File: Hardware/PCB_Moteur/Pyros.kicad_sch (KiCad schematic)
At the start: 33 parts, among them J8 Screw_Terminal_01x04, Q1 MMBT3904, Q2 SI7617DN-T1-GE3, Q3 SI5442DU-T1-GE3, Q4 SI5442DU-T1-GE3, U3 LM393

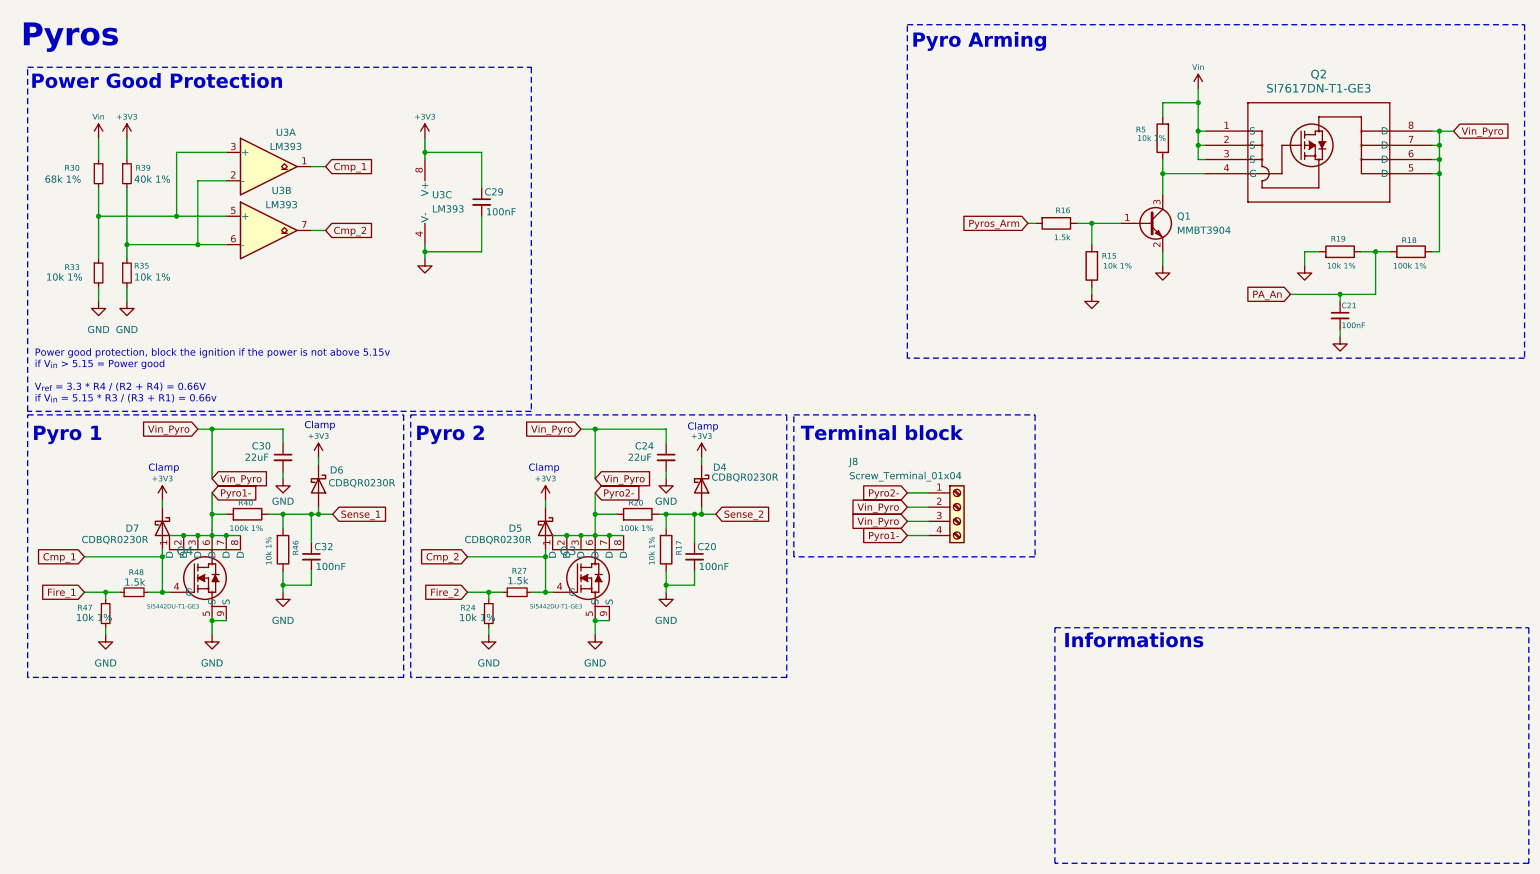
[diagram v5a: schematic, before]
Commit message: wip(moteur): reimport SI7617DN-T1-GE3 footprint + fix pads
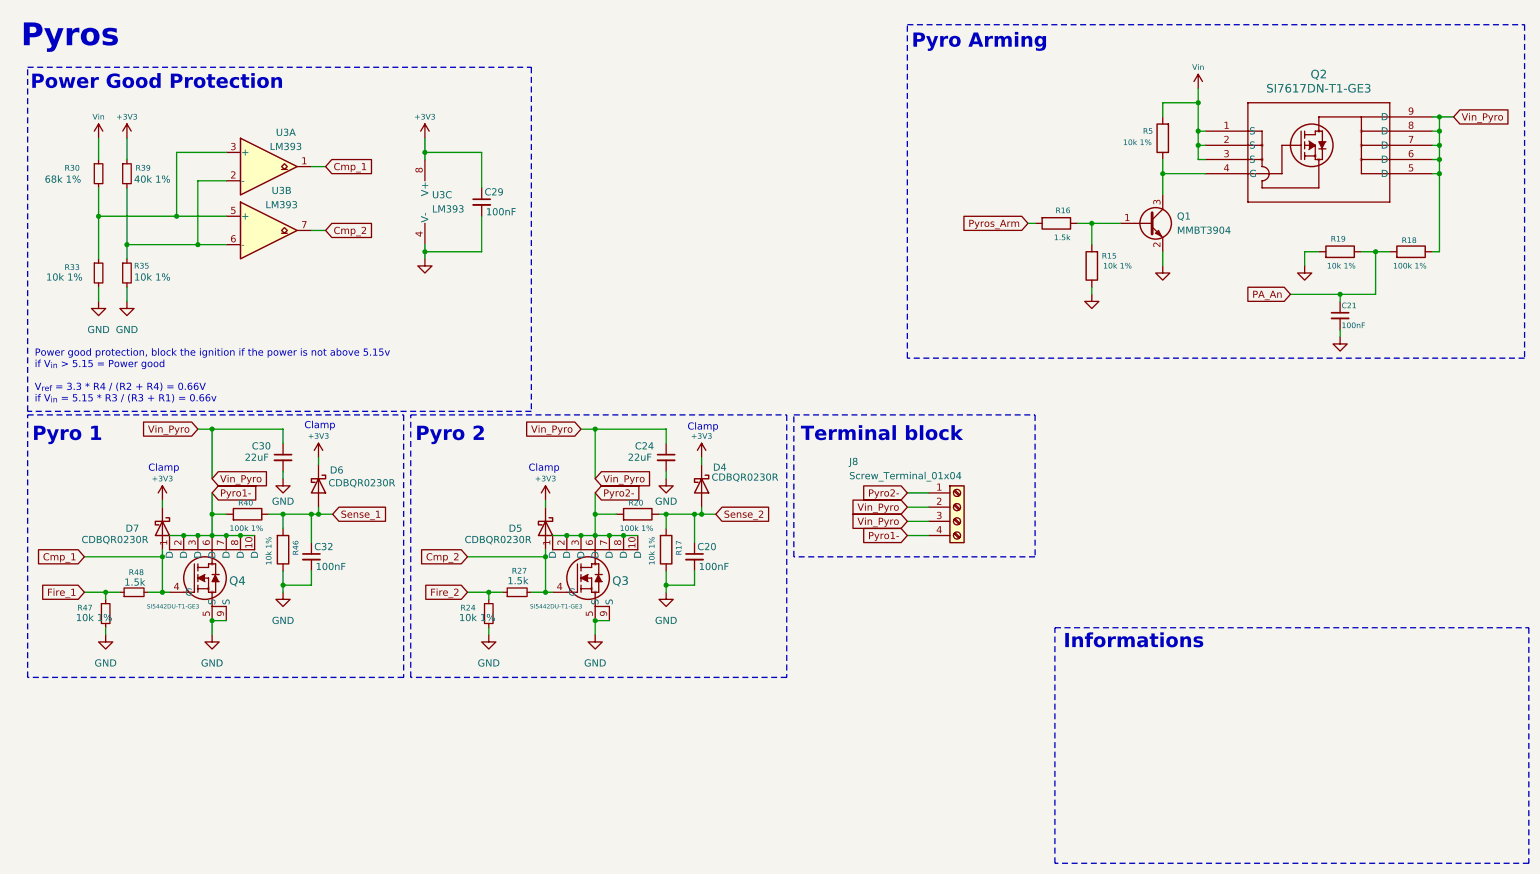
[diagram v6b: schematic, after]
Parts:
- Q2: footprint pcb_moteur:SI7617DN-T1-GE3 -> pcb_moteur:POWERPAK_1212-8_VIS
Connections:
- net Pyro1-: now also Q4.10 (D)
- net Pyro2-: now also Q3.10 (D)
- net Vin_Pyro: now also Q2.9 (D)
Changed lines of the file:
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@@
 	)
 	(junction
+		(at 266.7 30.48)
+		(diameter 0)
+		(color 0 0 0 0)
+	)
+	(junction
 		(at 113.03 105.41)
 		(diameter 0)
@@
 	)
 	(junction
+		(at 120.65 105.41)
+		(diameter 0)
+		(color 0 0 0 0)
+	)
+	(junction
 		(at 266.7 38.1)
 		(diameter 0)
@@
 	)
 	(junction
+		(at 52.07 105.41)
+		(diameter 0)
+		(color 0 0 0 0)
+	)
+	(junction
 		(at 128.27 114.3)
 		(diameter 0)
@@
 	(wire
 		(pts
+			(xy 120.65 105.41) (xy 123.19 105.41)
+		)
+		(stroke
+			(width 0)
+			(type default)
+		)
+	)
+	(wire
+		(pts
 			(xy 38.1 109.22) (xy 38.1 115.57)
 		)
@@
 	(wire
 		(pts
+			(xy 266.7 30.48) (xy 266.7 33.02)
+		)
+		(stroke
+			(width 0)
+			(type default)
+		)
+	)
+	(wire
+		(pts
 			(xy 95.25 36.83) (xy 85.09 36.83)
 		)
@@
 	(wire
 		(pts
-			(xy 266.7 33.02) (xy 269.24 33.02)
+			(xy 266.7 30.48) (xy 269.24 30.48)
 		)
 		(stroke
@@
 	(wire
 		(pts
+			(xy 52.07 105.41) (xy 54.61 105.41)
+		)
+		(stroke
+			(width 0)
+			(type default)
+		)
+	)
+	(wire
+		(pts
 			(xy 171.45 102.87) (xy 175.26 102.87)
 		)
@@
 	(wire
 		(pts
+			(xy 265.43 30.48) (xy 266.7 30.48)
+		)
+		(stroke
+			(width 0)
+			(type default)
+		)
+	)
+	(wire
+		(pts
 			(xy 115.57 97.79) (xy 115.57 101.6)
 		)
@@
 	(global_label "Vin_Pyro"
 		(shape input)
-		(at 269.24 33.02 0)
+		(at 269.24 30.48 0)
 		(fields_autoplaced yes)
 		(effects
@@
 		)
 		(property "Intersheetrefs" "${INTERSHEET_REFS}"
-			(at 280.208 33.02 0)
+			(at 280.208 30.48 0)
 			(effects
 				(font
@@
 		(dnp no)
 		(property "Reference" "R5"
-			(at 212.344 32.766 0)
+			(at 213.614 33.02 0)
 			(effects
 				(font
@@
 		)
 		(property "Value" "10k 1%"
-			(at 212.598 34.29 0)
+			(at 210.058 35.052 0)
 			(effects
 				(font
@@
 	)
 	(symbol
+		(lib_name "SI5442DU-T1-GE3_1")
 		(lib_id "pcb_moteur:SI5442DU-T1-GE3")
 		(at 107.95 115.57 0)
@@
 		(dnp no)
 		(property "Reference" "Q3"
-			(at 109.22 108.204 0)
+			(at 118.618 113.538 0)
 			(effects
 				(font
@@
 		(pin "2"
 		)
+		(pin "10"
+		)
 		(instances
 			(project "PCB_moteur"
@@
 			)
 		)
-		(property "Footprint" "pcb_moteur:SI7617DN-T1-GE3"
+		(property "Footprint" "pcb_moteur:POWERPAK_1212-8_VIS"
 			(at 224.79 33.02 0)
 			(effects
@@
 			)
 		)
-		(property "Datasheet" "https://www.digikey.ca/en/products/detail/vishay-siliconix/SI7617DN-T1-GE3/2441735"
+		(property "Datasheet" "https://www.vishay.com/doc?65164"
 			(at 224.79 33.02 0)
 			(effects
@@
 		(pin "6"
 		)
+		(pin "9"
+		)
 		(instances
 			(project ""
@@
 		(dnp no)
 		(property "Reference" "Q4"
-			(at 40.64 108.204 0)
+			(at 50.038 113.538 0)
 			(effects
 				(font
@@
 		(pin "6"
 		)
+		(pin "10"
+		)
 		(instances

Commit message: fix : BOM errors, change cutoff freq for moteur, minor fixes for GSE
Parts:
- R16, R27, R48: DigiKey_Part_Number P1.5KDBCT-ND -> 311-1.50KCRCT-ND; Manufacturer_Part_Number ERA-3AEB152V -> RC0805FR-071K5L
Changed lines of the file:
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@@
 			)
 		)
-		(property "Datasheet" "https://www.vishay.com/doc?65164"
+		(property "Datasheet" "https://www.digikey.com/en/products/detail/vishay-siliconix/SI7617DN-T1-GE3/2441735?s=N4IgTCBcDaIMoEkDsA2AjEgIgOQLQBU1cBxAUQGYBhfXbTEAXQF8g"
 			(at 224.79 33.02 0)
 			(effects
@@
 			)
 		)
-		(property "Datasheet" "https://www.digikey.ca/en/products/detail/panasonic-electronic-components/ERA-3AEB152V/1465858"
+		(property "Datasheet" "https://www.digikey.ca/en/products/detail/yageo/RC0805FR-071K5L/727496"
 			(at 101.6 115.57 0)
 			(effects
@@
 			)
 		)
-		(property "DigiKey_Part_Number" "P1.5KDBCT-ND"
+		(property "DigiKey_Part_Number" "311-1.50KCRCT-ND"
 			(at 101.6 115.57 90)
 			(effects
@@
 			)
 		)
-		(property "Manufacturer_Part_Number" "ERA-3AEB152V"
+		(property "Manufacturer_Part_Number" "RC0805FR-071K5L"
 			(at 101.6 115.57 90)
 			(effects
@@
 			)
 		)
-		(property "Datasheet" "https://www.digikey.ca/en/products/detail/panasonic-electronic-components/ERA-3AEB152V/1465858"
+		(property "Datasheet" "https://www.digikey.ca/en/products/detail/yageo/RC0805FR-071K5L/727496"
 			(at 198.12 49.53 0)
 			(effects
@@
 			)
 		)
-		(property "DigiKey_Part_Number" "P1.5KDBCT-ND"
+		(property "DigiKey_Part_Number" "311-1.50KCRCT-ND"
 			(at 198.12 49.53 90)
 			(effects
@@
 			)
 		)
-		(property "Manufacturer_Part_Number" "ERA-3AEB152V"
+		(property "Manufacturer_Part_Number" "RC0805FR-071K5L"
 			(at 198.12 49.53 90)
 			(effects
@@
 			)
 		)
-		(property "Datasheet" "https://www.digikey.ca/en/products/detail/panasonic-electronic-components/ERA-3AEB152V/1465858"
+		(property "Datasheet" "https://www.digikey.ca/en/products/detail/yageo/RC0805FR-071K5L/727496"
 			(at 33.02 115.57 0)
 			(effects
@@
 			)
 		)
-		(property "DigiKey_Part_Number" "P1.5KDBCT-ND"
+		(property "DigiKey_Part_Number" "311-1.50KCRCT-ND"
 			(at 33.02 115.57 90)
 			(effects
@@
 			)
 		)
-		(property "Manufacturer_Part_Number" "ERA-3AEB152V"
+		(property "Manufacturer_Part_Number" "RC0805FR-071K5L"
 			(at 33.02 115.57 90)
 			(effects

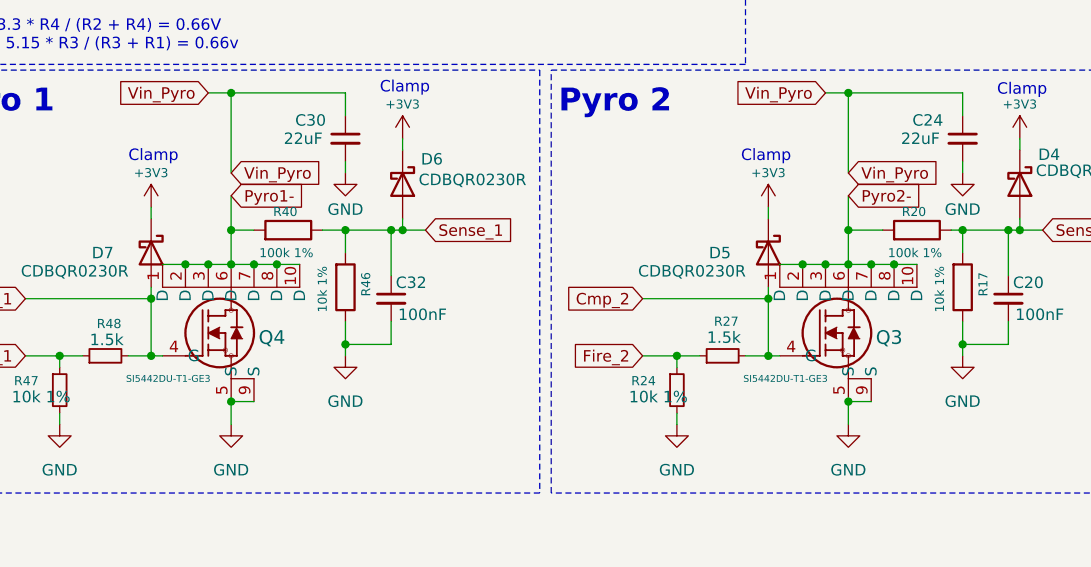
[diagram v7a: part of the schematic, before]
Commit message: fix(moteur): mosfet pyros pads
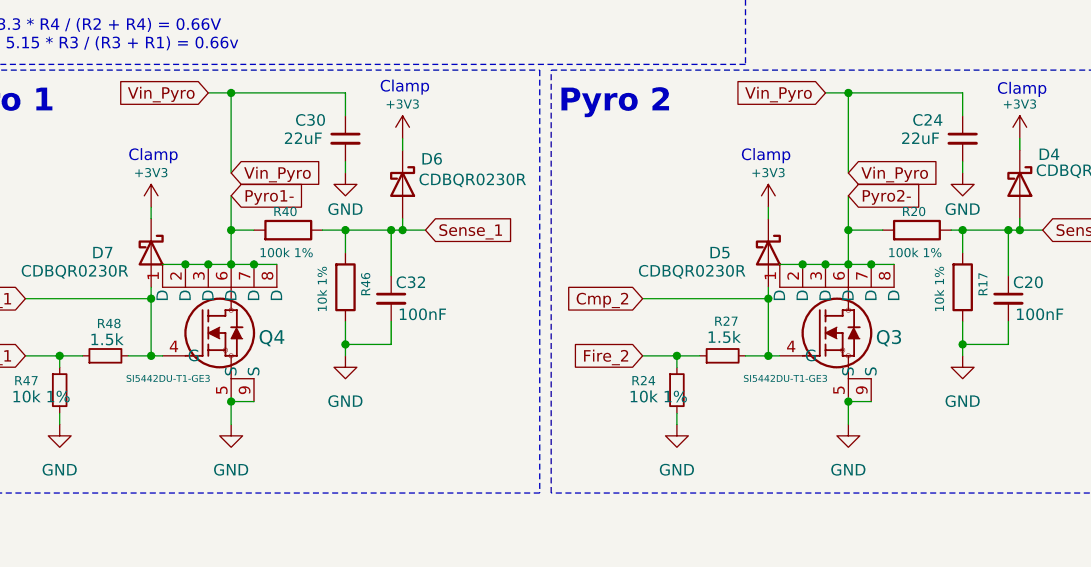
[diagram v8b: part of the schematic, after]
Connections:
- net Pyro1-: no longer Q4.10 (D)
- net Pyro2-: no longer Q3.10 (D)
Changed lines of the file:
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@@
 	)
 	(junction
-		(at 120.65 105.41)
-		(diameter 0)
-		(color 0 0 0 0)
-	)
-	(junction
 		(at 266.7 38.1)
 		(diameter 0)
@@
 	)
 	(junction
-		(at 52.07 105.41)
-		(diameter 0)
-		(color 0 0 0 0)
-	)
-	(junction
 		(at 128.27 114.3)
 		(diameter 0)
@@
 	(wire
 		(pts
-			(xy 120.65 105.41) (xy 123.19 105.41)
-		)
-		(stroke
-			(width 0)
-			(type default)
-		)
-	)
-	(wire
-		(pts
 			(xy 38.1 109.22) (xy 38.1 115.57)
 		)
@@
 	(wire
 		(pts
-			(xy 52.07 105.41) (xy 54.61 105.41)
-		)
-		(stroke
-			(width 0)
-			(type default)
-		)
-	)
-	(wire
-		(pts
 			(xy 171.45 102.87) (xy 175.26 102.87)
 		)
@@
 		(pin "2"
 		)
-		(pin "10"
-		)
 		(instances
 			(project "PCB_moteur"
@@
 		(pin "6"
 		)
-		(pin "10"
-		)
 		(instances
